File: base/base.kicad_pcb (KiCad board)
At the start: 2 copper layers, 51.2 x 20.5 mm, 12 parts, among them J1 Game Boy, J2 Game Gear, J3 Programming, U1 HC139, U2 PIC10F200-IOT

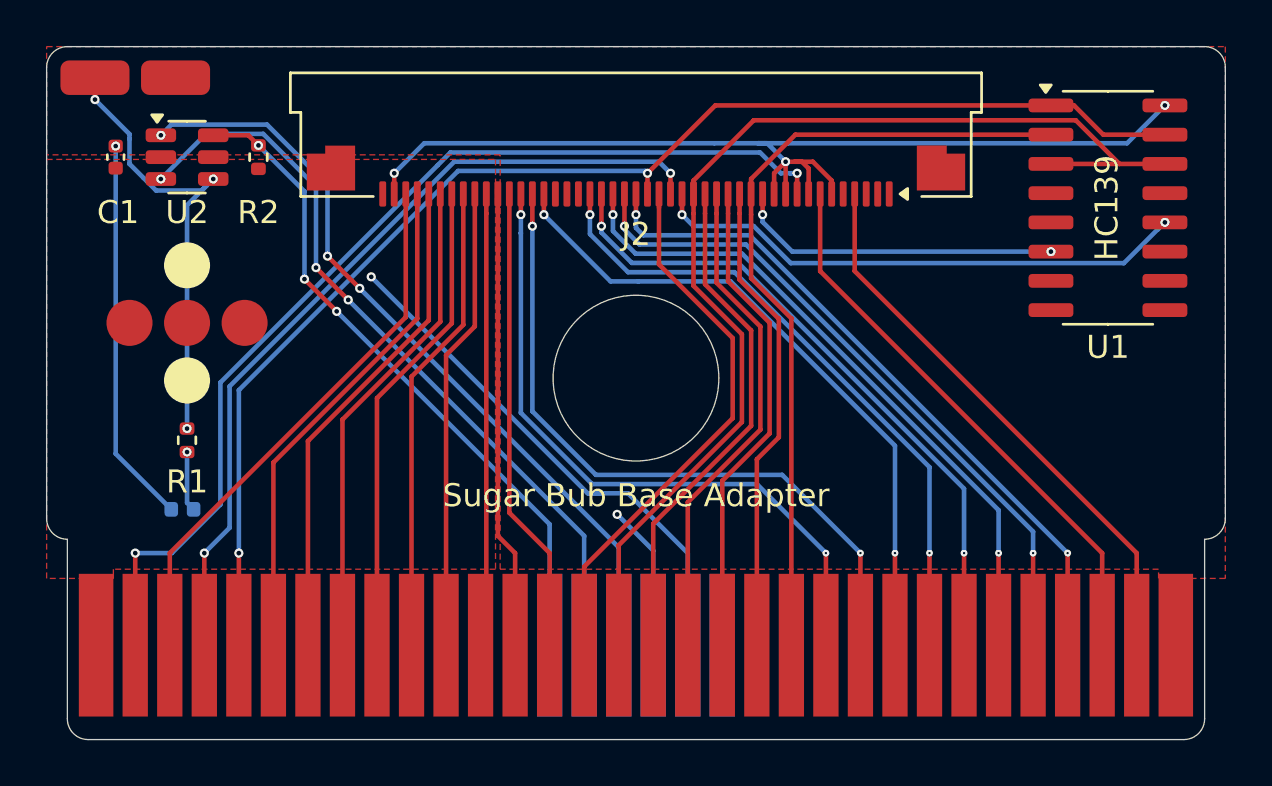
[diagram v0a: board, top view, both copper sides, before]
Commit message: Widen via holes
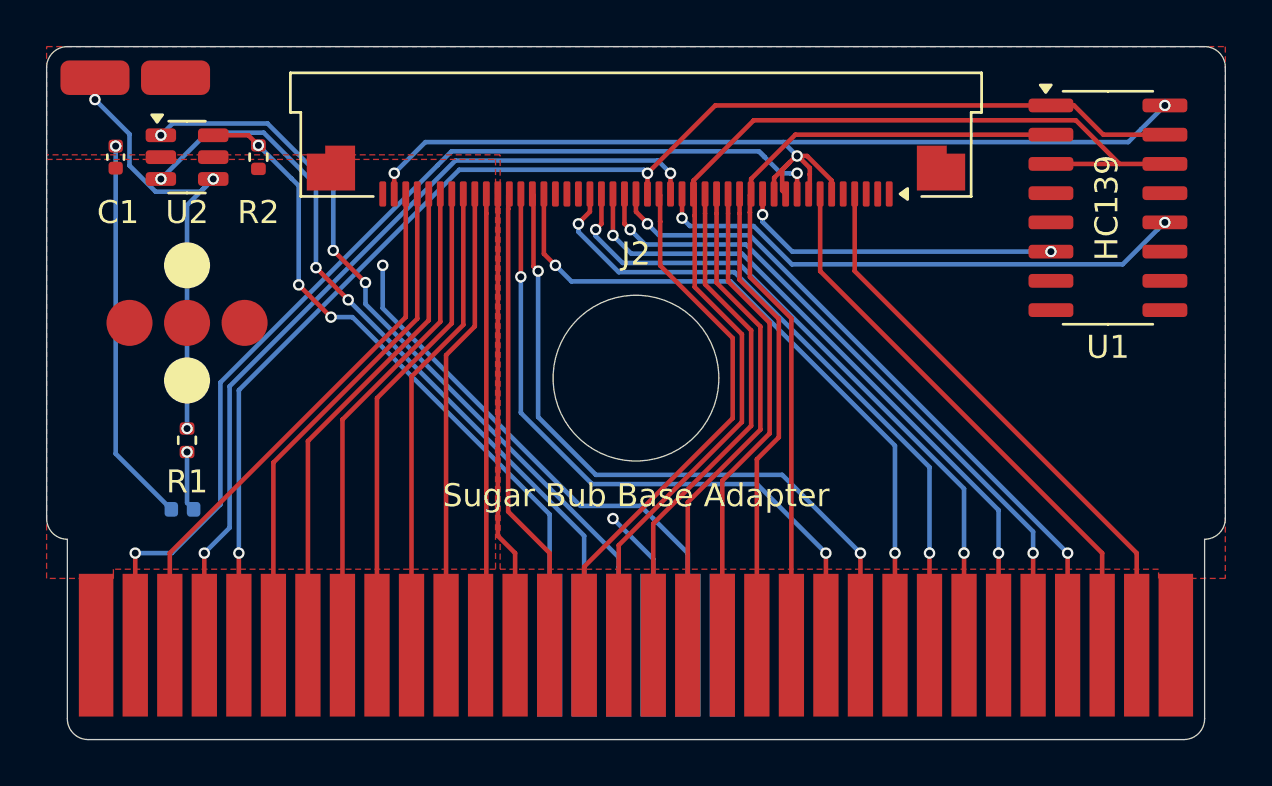
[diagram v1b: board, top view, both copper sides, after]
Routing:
- net /D2: track 29.0 -> 30.0 mm
- net /D3: track 28.4 -> 29.1 mm
- net Net-(J3-Pin_6): track 29.1 -> 29.6 mm
